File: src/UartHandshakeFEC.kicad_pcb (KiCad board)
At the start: 2 copper layers, 24 x 22.8 mm, 18 parts, among them J1 B3B-XH-A, P1 105444-0001, U1 FT232RL

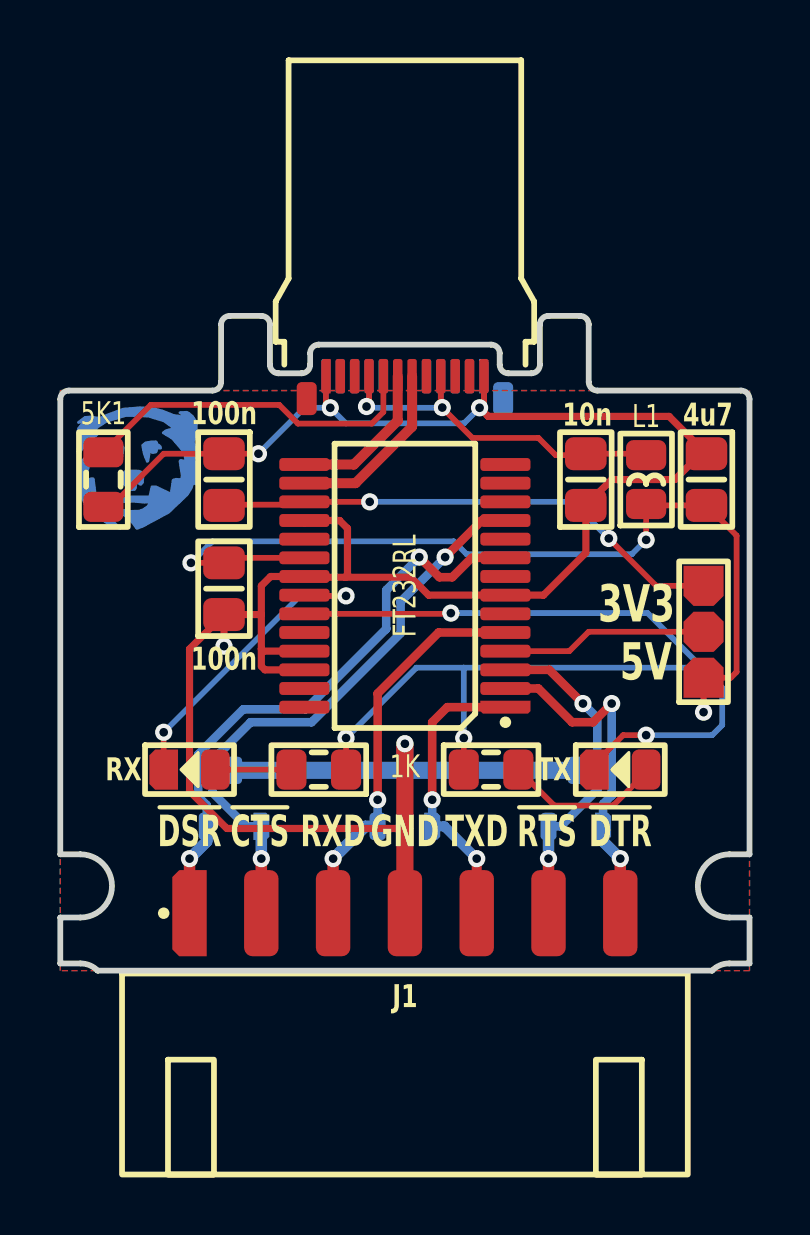
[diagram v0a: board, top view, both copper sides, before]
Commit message: Updated pinout to match cisco-style pin order
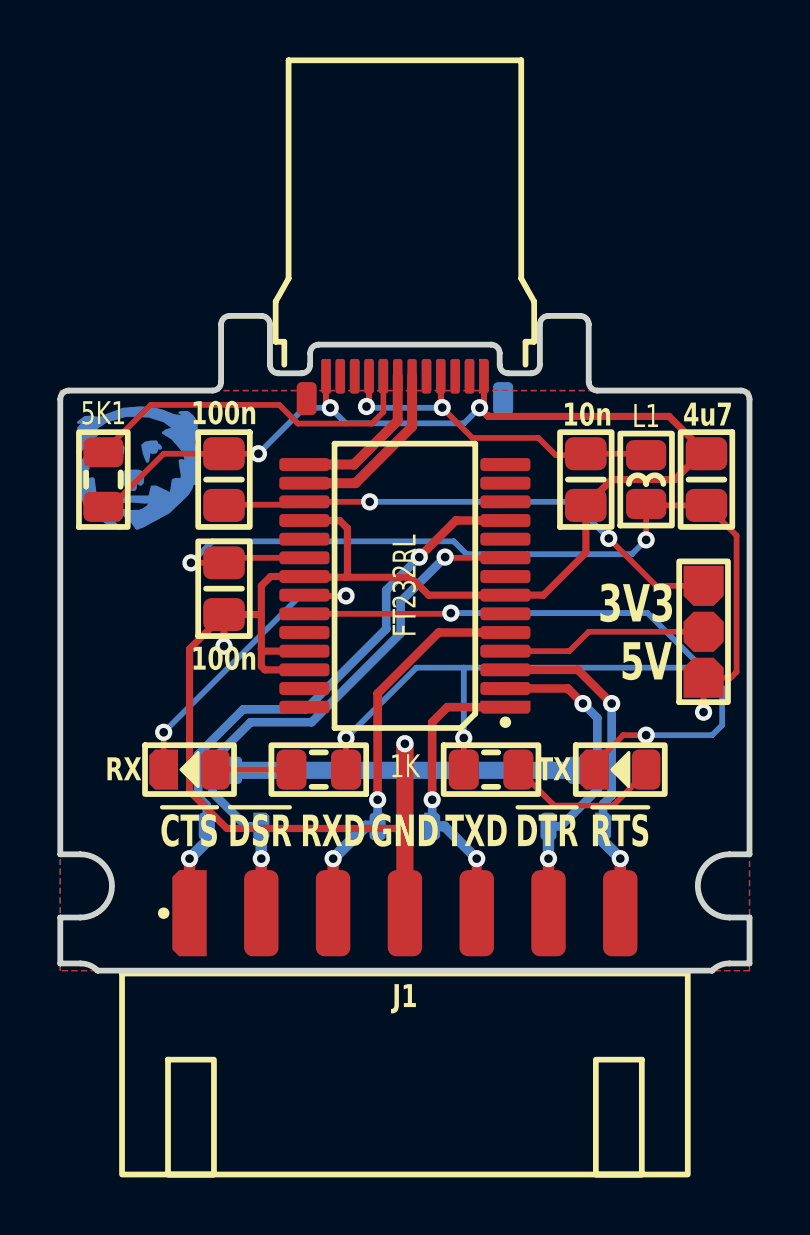
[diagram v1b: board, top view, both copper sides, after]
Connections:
- D1 pad 1: DTR# -> RTS#
- D1 pad 2: RTS# -> DTR#
- D3 pad 1: CTS# -> DSR#
- D3 pad 2: DSR# -> CTS#
- J1 pad 1: DSR# -> CTS#
- J1 pad 2: CTS# -> DSR#
- J1 pad 6: RTS# -> DTR#
- J1 pad 7: DTR# -> RTS#
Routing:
- net DTR#: track 12.2 -> 11.4 mm
- net DSR#: track 20.8 -> 20.1 mm

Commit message: Refactoring LEDs to bottom
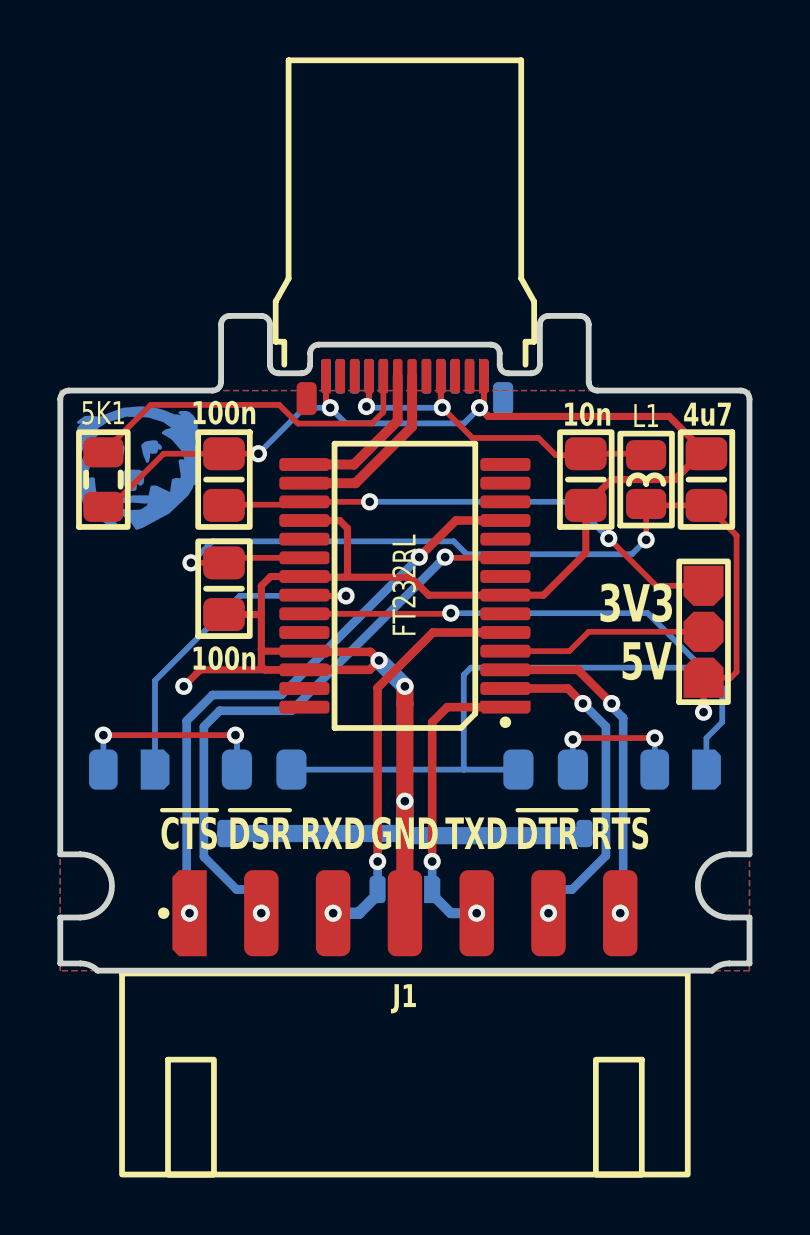
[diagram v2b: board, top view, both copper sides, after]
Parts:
- DS1, DS2, R1, R2: moved to B.Cu
- J1: value B3B-XH-A -> B7B-XH-A
- moved D3 2.22 mm to (25.8, 39.0)
- moved D1 2.22 mm to (38.2, 39.0)
- moved D2 2.20 mm to (32.0, 39.0)
- moved DS1 2.10 mm to (22.4, 35.8), turned to 180 degrees
- moved DS2 2.10 mm to (41.6, 35.8), turned to 180 degrees
- moved R1 1.90 mm to (27.1, 35.8)
- moved R2 1.90 mm to (36.9, 35.8)
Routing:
- net LED_RXD': track 2.65 -> 7.02 mm, vias 0 -> 2
- net LED_TXD: track 21.9 -> 18.7 mm, vias 2 -> 1
- net GND: track 92.8 -> 91.0 mm, vias 5 -> 7
- net 5V: track 51.6 -> 53.1 mm, vias 5 -> 3
- net LED_RXD: track 11.0 -> 12.4 mm, vias 2 -> 1
- net LED_TXD': track 5.44 -> 5.09 mm, vias 0 -> 2
